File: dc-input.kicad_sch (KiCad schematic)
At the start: 4 parts, among them J11 BarrelJack_3167288

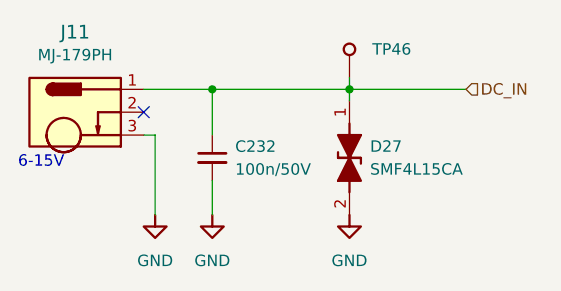
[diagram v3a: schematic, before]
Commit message: [#56935] Update symbol/footprint links; Migrate to KiCad 7
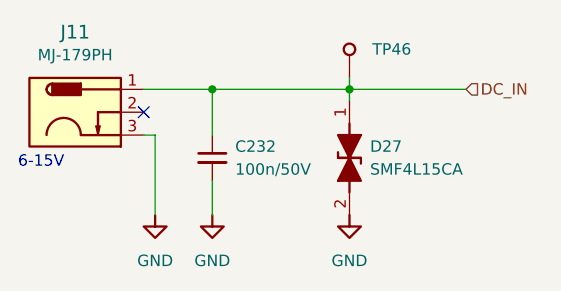
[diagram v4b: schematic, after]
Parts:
- C232: footprint kria-k26-devboard-footprints:C_0402_1005Metric -> antmicro-footprints:C_0402_1005Metric; symbol kria-k26-devboard:C_100n_50V_0402 -> antmicroCapacitorsmisc:C_100n_50V_0402
- D27: footprint kria-k26-devboard-footprints:SOD-123FL -> antmicro-footprints:SOD-123FL; symbol kria-k26-devboard:SMF4L15CA -> antmicroTVSDiodes:SMF4L15CA
- J11: footprint kria-k26-devboard-footprints:BarrelJack_3167288_Horizontal -> antmicro-footprints:BarrelJack_Pin2mm_MJ-179PH; symbol kria-k26-devboard:BarrelJack_3167288 -> antmicroBarrelPowerConnectors:BarrelJack_Pin2mm_MJ-179PH
- TP46: footprint kria-k26-devboard-footprints:TP_SMD_0.75mm -> antmicro-footprints:TP_SMD_0.75mm; symbol kria-k26-devboard:TP_0.75mm_SMD -> antmicroTestPoints:TP_0.75mm_SMD

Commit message: [#56935] Fix missing highlights in OHP
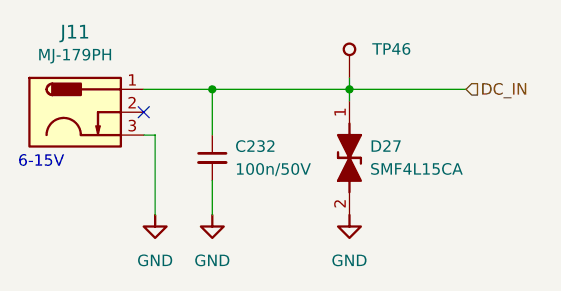
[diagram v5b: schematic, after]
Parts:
- J11: value BarrelJack_3167288 -> BarrelJack_Pin2mm_MJ-179PH; Manufacturer Multicomp -> Multicomp Pro
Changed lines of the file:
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@@
     )
   )
-  (symbol (lib_id "antmicroBarrelPowerConnectors:BarrelJack_Pin2mm_MJ-179PH") (at 144.78 88.9 0) (mirror y) (unit 1)
-    (in_bom yes) (on_board yes) (dnp no)
+  (symbol (lib_id "antmicroBarrelPowerConnectors:BarrelJack_Pin2mm_MJ-179PH") (at 144.78 88.9 0) (unit 1)
+    (in_bom yes) (on_board yes) (dnp no) (fields_autoplaced)
     (property "Reference" "J11" (at 137.16 82.55 0)
       (effects (font (size 1.524 1.524)))
     )
-    (property "Value" "BarrelJack_3167288" (at 137.16 85.09 0)
+    (property "Value" "BarrelJack_Pin2mm_MJ-179PH" (at 152.4 85.09 0)
       (effects (font (size 1.27 1.27) (thickness 0.15)) hide)
     )
-    (property "Footprint" "antmicro-footprints:BarrelJack_Pin2mm_MJ-179PH" (at 143.51 97.79 0)
+    (property "Footprint" "antmicro-footprints:BarrelJack_Pin2mm_MJ-179PH" (at 146.05 97.79 0)
       (effects (font (size 1.27 1.27) (thickness 0.15)) (justify left bottom) hide)
     )
@@
       (effects (font (size 1.27 1.27) (thickness 0.15)) (justify left bottom) hide)
     )
-    (property "Manufacturer" "Multicomp" (at 144.145 100.965 0)
+    (property "Manufacturer" "Multicomp Pro" (at 145.415 100.965 0)
       (effects (font (size 1.27 1.27) (thickness 0.15)) (justify left bottom) hide)
     )
@@
       (effects (font (size 1.27 1.27) (thickness 0.15)))
     )
-    (property "Author" "Antmicro" (at 127 109.22 0)
+    (property "Author" "Antmicro" (at 162.56 109.22 0)
       (effects (font (size 1.27 1.27) (thickness 0.15)) (justify left bottom) hide)
     )
-    (property "License" "Apache-2.0" (at 127 111.76 0)
+    (property "License" "Apache-2.0" (at 162.56 111.76 0)
       (effects (font (size 1.27 1.27) (thickness 0.15)) (justify left bottom) hide)
     )

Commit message: [#56935] Loclib
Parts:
- C232: footprint antmicro-footprints:C_0402_1005Metric -> kria-k26-devboard-footprints:C_0402_1005Metric; symbol antmicroCapacitorsmisc:C_100n_50V_0402 -> kria-k26-devboard:C_100n_50V_0402
- D27: footprint antmicro-footprints:SOD-123FL -> kria-k26-devboard-footprints:SOD-123FL; symbol antmicroTVSDiodes:SMF4L15CA -> kria-k26-devboard:SMF4L15CA
- J11: footprint antmicro-footprints:BarrelJack_Pin2mm_MJ-179PH -> kria-k26-devboard-footprints:BarrelJack_Pin2mm_MJ-179PH; symbol antmicroBarrelPowerConnectors:BarrelJack_Pin2mm_MJ-179PH -> kria-k26-devboard:BarrelJack_Pin2mm_MJ-179PH
- TP46: footprint antmicro-footprints:TP_SMD_0.75mm -> kria-k26-devboard-footprints:TP_SMD_0.75mm; symbol antmicroTestPoints:TP_0.75mm_SMD -> kria-k26-devboard:TP_0.75mm_SMD
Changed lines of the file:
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@@
     (effects (font (size 1.27 1.27)) (justify left))
   )
-  (symbol (lib_id "antmicroTVSDiodes:SMF4L15CA") (at 167.64 90.17 270) (unit 1)
+  (symbol (lib_id "kria-k26-devboard:SMF4L15CA") (at 167.64 90.17 270) (unit 1)
     (in_bom yes) (on_board yes) (dnp no) (fields_autoplaced)
     (property "Reference" "D27" (at 169.926 95.2499 90)
@@
       (effects (font (size 1.27 1.27) (thickness 0.15)) (justify left))
     )
-    (property "Footprint" "antmicro-footprints:SOD-123FL" (at 167.64 90.17 0)
+    (property "Footprint" "kria-k26-devboard-footprints:SOD-123FL" (at 167.64 90.17 0)
       (effects (font (size 1.27 1.27) (thickness 0.15)) (justify left bottom) hide)
     )
@@
     )
   )
-  (symbol (lib_id "antmicroBarrelPowerConnectors:BarrelJack_Pin2mm_MJ-179PH") (at 144.78 88.9 0) (unit 1)
+  (symbol (lib_id "kria-k26-devboard:BarrelJack_Pin2mm_MJ-179PH") (at 144.78 88.9 0) (unit 1)
     (in_bom yes) (on_board yes) (dnp no) (fields_autoplaced)
     (property "Reference" "J11" (at 137.16 82.55 0)
@@
       (effects (font (size 1.27 1.27) (thickness 0.15)) hide)
     )
-    (property "Footprint" "antmicro-footprints:BarrelJack_Pin2mm_MJ-179PH" (at 146.05 97.79 0)
+    (property "Footprint" "kria-k26-devboard-footprints:BarrelJack_Pin2mm_MJ-179PH" (at 146.05 97.79 0)
       (effects (font (size 1.27 1.27) (thickness 0.15)) (justify left bottom) hide)
     )
@@
     )
   )
-  (symbol (lib_id "antmicropower:GND") (at 146.05 102.87 0) (unit 1)
+  (symbol (lib_id "kria-k26-devboard:GND") (at 146.05 102.87 0) (unit 1)
     (in_bom yes) (on_board yes) (dnp no) (fields_autoplaced)
     (property "Reference" "#PWR0396" (at 146.05 109.22 0)
@@
     )
   )
-  (symbol (lib_id "antmicroCapacitorsmisc:C_100n_50V_0402") (at 152.4 93.98 270) (unit 1)
+  (symbol (lib_id "kria-k26-devboard:C_100n_50V_0402") (at 152.4 93.98 270) (unit 1)
     (in_bom yes) (on_board yes) (dnp no) (fields_autoplaced)
     (property "Reference" "C232" (at 154.94 95.2562 90)
@@
       (effects (font (size 1.27 1.27) (thickness 0.15)) (justify left bottom) hide)
     )
-    (property "Footprint" "antmicro-footprints:C_0402_1005Metric" (at 152.4 93.98 0)
+    (property "Footprint" "kria-k26-devboard-footprints:C_0402_1005Metric" (at 152.4 93.98 0)
       (effects (font (size 1.27 1.27) (thickness 0.15)) (justify left bottom) hide)
     )
@@
     )
   )
-  (symbol (lib_id "antmicroTestPoints:TP_0.75mm_SMD") (at 167.64 87.63 90) (unit 1)
+  (symbol (lib_id "kria-k26-devboard:TP_0.75mm_SMD") (at 167.64 87.63 90) (unit 1)
     (in_bom yes) (on_board yes) (dnp no) (fields_autoplaced)
     (property "Reference" "TP46" (at 170.18 84.4549 90)
@@
       (effects (font (size 1.27 1.27) (thickness 0.15)) (justify left bottom) hide)
     )
-    (property "Footprint" "antmicro-footprints:TP_SMD_0.75mm" (at 162.56 82.55 0)
+    (property "Footprint" "kria-k26-devboard-footprints:TP_SMD_0.75mm" (at 162.56 82.55 0)
       (effects (font (size 1.27 1.27) (thickness 0.15)) (justify left bottom) hide)
     )
@@
     )
   )
-  (symbol (lib_id "antmicropower:GND") (at 167.64 102.87 0) (unit 1)
+  (symbol (lib_id "kria-k26-devboard:GND") (at 167.64 102.87 0) (unit 1)
     (in_bom yes) (on_board yes) (dnp no) (fields_autoplaced)
     (property "Reference" "#PWR0107" (at 167.64 109.22 0)
@@
     )
   )
-  (symbol (lib_id "antmicropower:GND") (at 152.4 102.87 0) (unit 1)
+  (symbol (lib_id "kria-k26-devboard:GND") (at 152.4 102.87 0) (unit 1)
     (in_bom yes) (on_board yes) (dnp no) (fields_autoplaced)
     (property "Reference" "#PWR0104" (at 152.4 109.22 0)
